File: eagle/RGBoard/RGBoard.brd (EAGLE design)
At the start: 50 x 50 mm, 24 parts

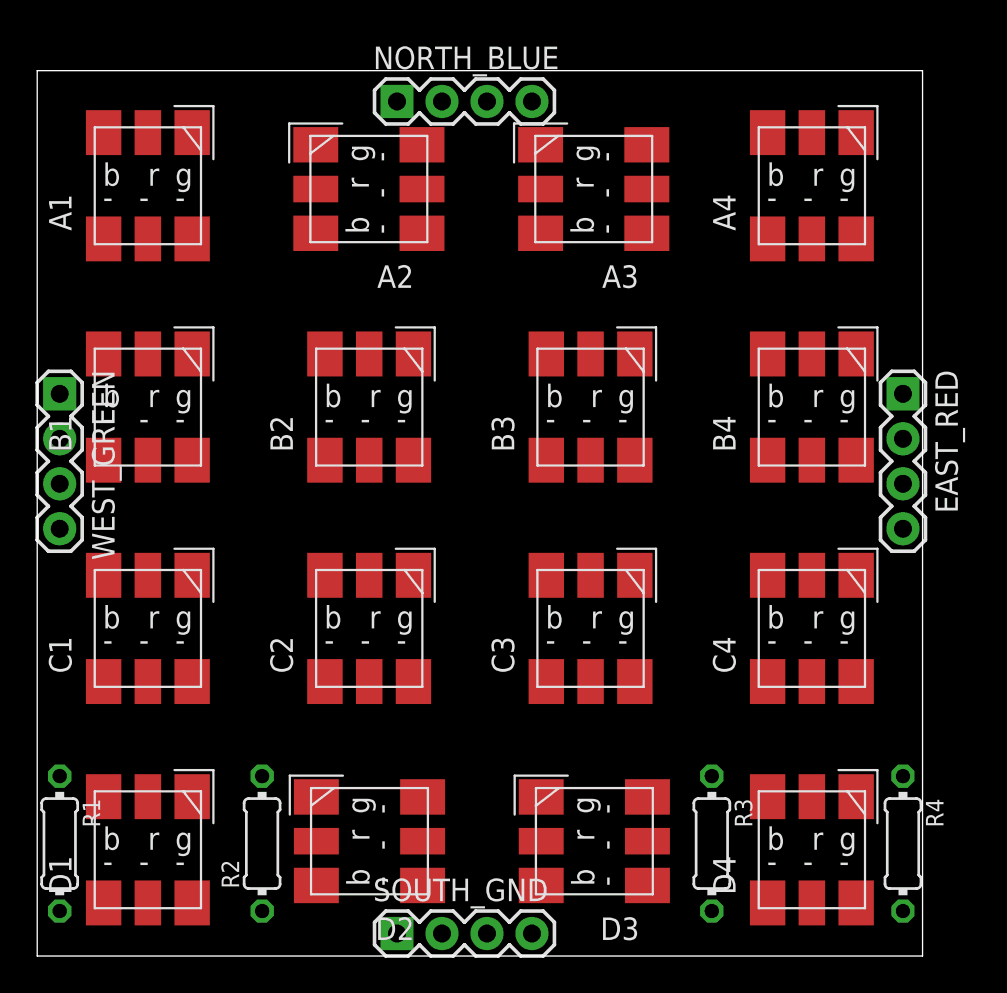
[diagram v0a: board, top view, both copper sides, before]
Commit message: Wiring ok, need refactor on silk before going to prod.
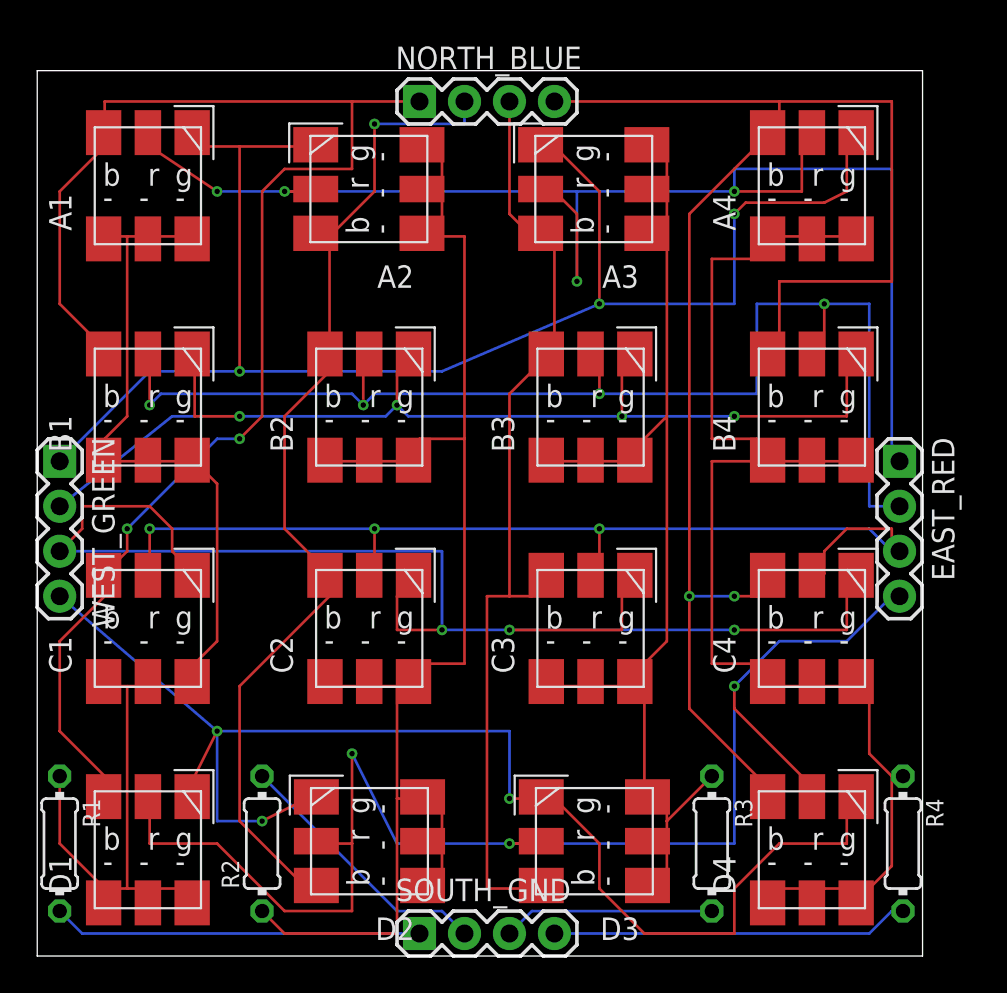
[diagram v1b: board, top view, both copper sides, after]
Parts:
- moved EAST_RED 3.81 mm to (48.7, 27.9)
- moved WEST_GREEN 3.81 mm to (1.27, 27.9)
- moved NORTH_BLUE 1.27 mm to (21.6, 48.3)
- moved SOUTH_GND 1.27 mm to (21.6, 1.27)
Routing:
- net N$12: track 0.00 -> 88.3 mm, vias 0 -> 2
- net N$13: track 0.00 -> 87.4 mm, vias 0 -> 3
- net N$9: track 0.00 -> 84.3 mm, vias 0 -> 2
- net GND2: track 0.00 -> 84.1 mm
- net N$8: track 0.00 -> 82.9 mm, vias 0 -> 3
- net N$5: track 0.00 -> 82.3 mm, vias 0 -> 4
- net N$15: track 0.00 -> 79.6 mm, vias 0 -> 3
- net N$16: track 0.00 -> 77.4 mm, vias 0 -> 3
- net GND4: track 0.00 -> 73.1 mm
- net N$6: track 0.00 -> 71.1 mm, vias 0 -> 4
- net GND1: track 0.00 -> 70.0 mm
- net GND3: track 0.00 -> 67.7 mm
- net N$14: track 0.00 -> 63.5 mm, vias 0 -> 4
- net N$7: track 0.00 -> 59.5 mm, vias 0 -> 3
- net N$10: track 0.00 -> 58.1 mm, vias 0 -> 1
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
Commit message: v1 sent to production
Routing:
- net N$14: track 63.5 -> 75.7 mm
- net N$6: track 71.1 -> 78.8 mm
- net N$10: track 58.1 -> 63.8 mm
- net N$13: track 87.4 -> 90.4 mm
- net N$8: track 82.9 -> 85.6 mm
- net N$11: track 54.4 -> 56.4 mm
- net N$5: track 82.3 -> 84.0 mm
- net N$9: track 84.3 -> 85.8 mm
- net N$15: track 79.6 -> 78.8 mm
- net N$7: track 59.5 -> 58.7 mm
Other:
- board text added: "#Order 46415"
- board text added: "A1"
- board text added: "A4"
- board text added: "BLUE1"
- board text added: "D1"
- board text added: "D4"
- board text added: "GND1"
- board text added: "GREEN1"
- board text added: "R1"
- board text added: "R2"
- board text added: "R3"
- board text added: "R4"
- board text added: "RED1"
- board text added: "http://kalshagar.wikispaces.com/RGBoard"
